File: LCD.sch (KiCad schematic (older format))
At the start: 7 parts

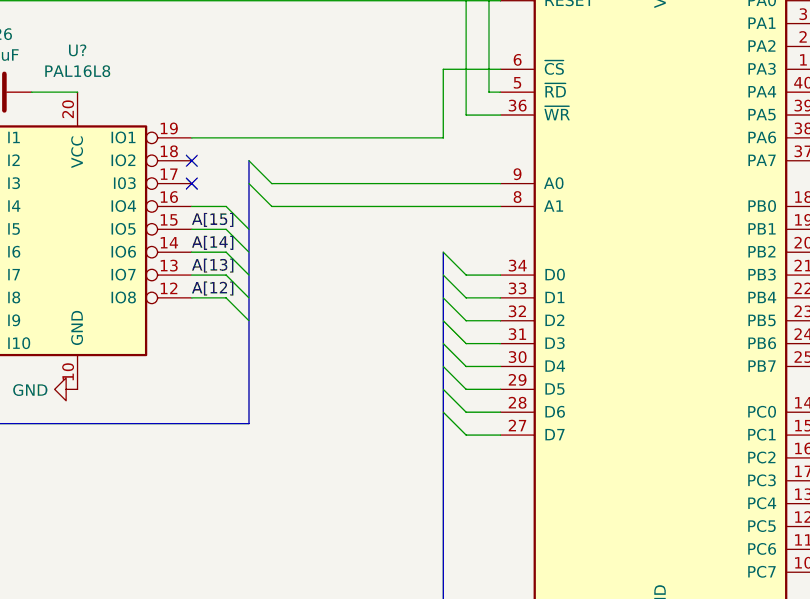
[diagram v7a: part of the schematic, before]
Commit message: Missed some labels
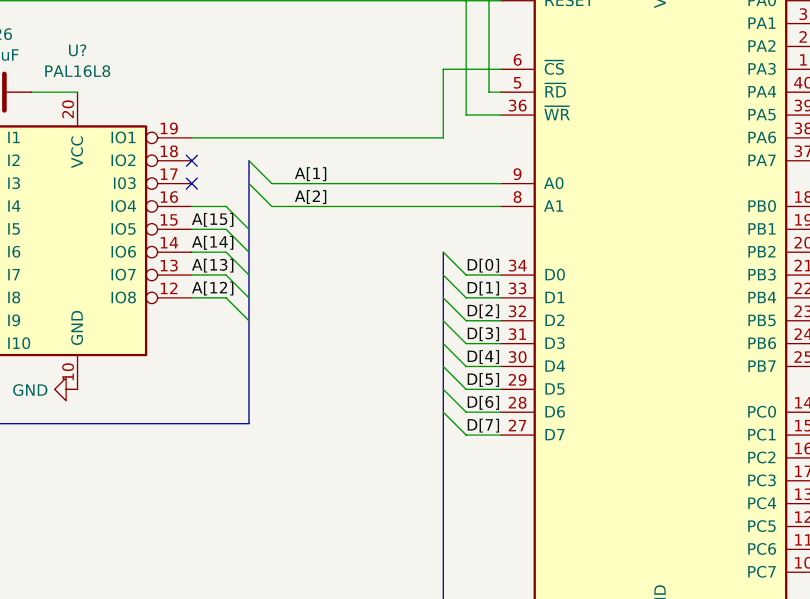
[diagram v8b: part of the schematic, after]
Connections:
- net D[7]: now reaches U?.27 (D7)
- net D[6]: now reaches U?.28 (D6)
- net D[5]: now reaches U?.29 (D5)
- net D[4]: now reaches U?.30 (D4)
- net D[3]: now reaches U?.31 (D3)
- net D[2]: now reaches U?.32 (D2)
- net D[1]: now reaches U?.33 (D1)
- net D[0]: now reaches U?.34 (D0)
- net A[2]: now reaches U?.8 (A1)
- net A[1]: now reaches U?.9 (A0)
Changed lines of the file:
@@
 Wire Bus Line
 	2250 3000 2250 4750
+Text Label 4000 3700 0    50   ~ 0
+A[1]
+Text Label 4000 3800 0    50   ~ 0
+A[2]
+Text Label 4750 4100 0    50   ~ 0
+D[0]
+Text Label 4750 4200 0    50   ~ 0
+D[1]
+Text Label 4750 4300 0    50   ~ 0
+D[2]
+Text Label 4750 4400 0    50   ~ 0
+D[3]
+Text Label 4750 4500 0    50   ~ 0
+D[4]
+Text Label 4750 4600 0    50   ~ 0
+D[5]
+Text Label 4750 4700 0    50   ~ 0
+D[6]
+Text Label 4750 4800 0    50   ~ 0
+D[7]
 $EndSCHEMATC
